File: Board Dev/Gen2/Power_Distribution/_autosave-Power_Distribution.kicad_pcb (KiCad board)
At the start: 2 copper layers, 155 x 59 mm, 26 parts, among them IC1 ACS713ELCTR-30A-T, IC2 ACS713ELCTR-30A-T, IC3 ACS713ELCTR-30A-T, IC4 ACS713ELCTR-30A-T, IC5 ACS713ELCTR-30A-T, IC6 ACS713ELCTR-30A-T, IC7 ACS713ELCTR-30A-T, IC8 ACS713ELCTR-30A-T, J1 8TERM_VERT_1719370, J2 8TERM_VERT_1719370

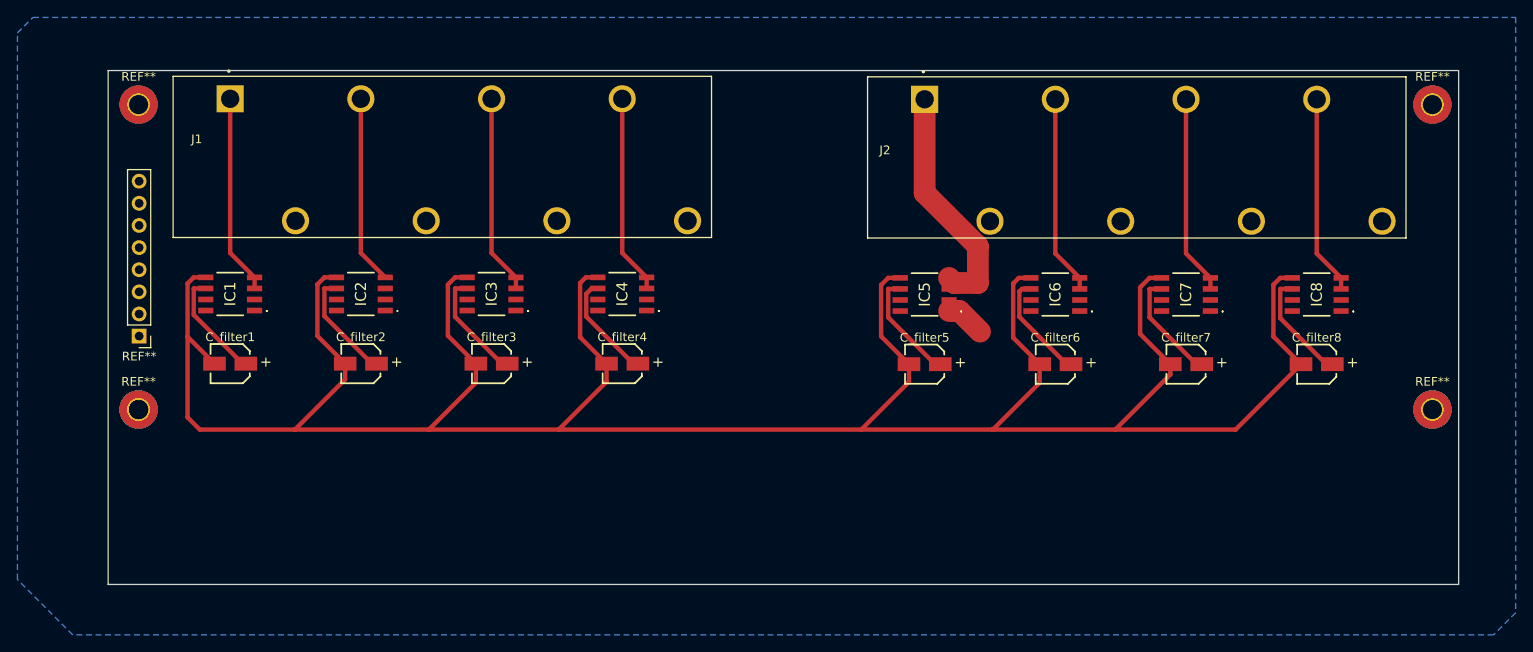
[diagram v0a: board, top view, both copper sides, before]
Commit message: draft of connecting board with current sensors
I'm still waiting to get an email back for the footprint of the connector pins but i have a good one saved.
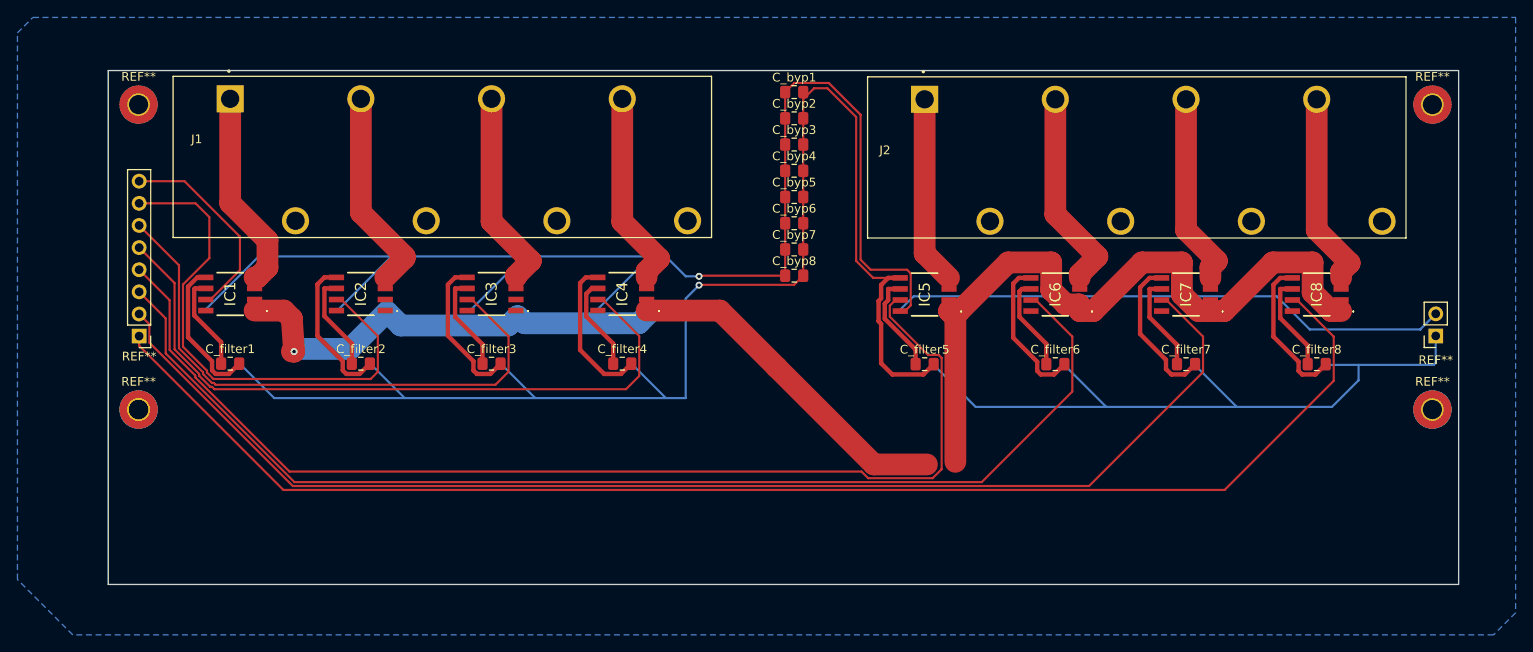
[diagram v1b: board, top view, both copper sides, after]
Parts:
- added C_byp1: 0.1 µF, Capacitor_SMD:C_0805_2012Metric_Pad1.18x1.45mm_HandSolder, F.Cu at (225.3, 92.4)
- added C_byp2: 0.1 µF, Capacitor_SMD:C_0805_2012Metric_Pad1.18x1.45mm_HandSolder, F.Cu at (225.3, 95.4)
- added C_byp3: 0.1 µF, Capacitor_SMD:C_0805_2012Metric_Pad1.18x1.45mm_HandSolder, F.Cu at (225.3, 98.4)
- added C_byp4: 0.1 µF, Capacitor_SMD:C_0805_2012Metric_Pad1.18x1.45mm_HandSolder, F.Cu at (225.3, 101.4)
- added C_byp5: 0.1 µF, Capacitor_SMD:C_0805_2012Metric_Pad1.18x1.45mm_HandSolder, F.Cu at (225.3, 104.4)
- added C_byp6: 0.1 µF, Capacitor_SMD:C_0805_2012Metric_Pad1.18x1.45mm_HandSolder, F.Cu at (225.3, 107.4)
- added C_byp7: 0.1 µF, Capacitor_SMD:C_0805_2012Metric_Pad1.18x1.45mm_HandSolder, F.Cu at (225.3, 110.5)
- added C_byp8: 0.1 µF, Capacitor_SMD:C_0805_2012Metric_Pad1.18x1.45mm_HandSolder, F.Cu at (225.3, 113.5)
- added REF**: PinSocket_1x02_P2.54mm_Vertical, Connector_PinSocket_2.54mm:PinSocket_1x02_P2.54mm_Vertical, F.Cu at (298.9, 120.4)
- C_filter1, C_filter2, C_filter3, C_filter4, C_filter5, C_filter6, C_filter7, C_filter8: footprint 0802 cap:0802 Cap -> Capacitor_SMD:C_0805_2012Metric_Pad1.18x1.45mm_HandSolder
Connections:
- REF** pad 1: (no net) -> VIout8
- REF** pad 2: (no net) -> VIout7
- REF** pad 3: (no net) -> VIout6
- REF** pad 4: (no net) -> VIout5
- REF** pad 5: (no net) -> VIout4
- REF** pad 6: (no net) -> VIout3
- REF** pad 7: (no net) -> VIout2
- REF** pad 8: (no net) -> VIout1
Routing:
- net 5V: track 0.00 -> 221.3 mm, vias 0 -> 1
- net +BATT: track 4.54 -> 175.9 mm, vias 0 -> 1
- net VIout8: track 0.00 -> 161.8 mm
- net VIout7: track 0.00 -> 147.5 mm
- net VIout6: track 0.00 -> 135.6 mm
- net VIout5: track 0.00 -> 129.3 mm
- net VIout4: track 0.00 -> 80.4 mm
- net VIout3: track 0.00 -> 66.9 mm
- net GND: track 303.4 -> 369.8 mm, vias 0 -> 1
- net VIout2: track 0.00 -> 59.8 mm
- net VIout1: track 0.00 -> 23.4 mm
- net PWR5: track 28.4 -> 22.9 mm
- net PWR2: track 21.7 -> 23.5 mm
- net PWR6: track 22.9 -> 24.6 mm
- net Net-(IC8-FILTER): track 12.9 -> 11.3 mm
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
